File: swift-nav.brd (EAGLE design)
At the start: 53 x 53 mm, 163 parts, among them J1 SMA_EDGE, J6 ZX62-B-5PA, U1 6SLX9FTG256, U10 MAX2769, U12 PT7M8206B33TA5EX, U13 M25PX80, U2 LTC3407A_DFN, U3 STM32-M-64-LQFP, U4 7Q-16.368MBG-T, U5 SMA_PATCH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

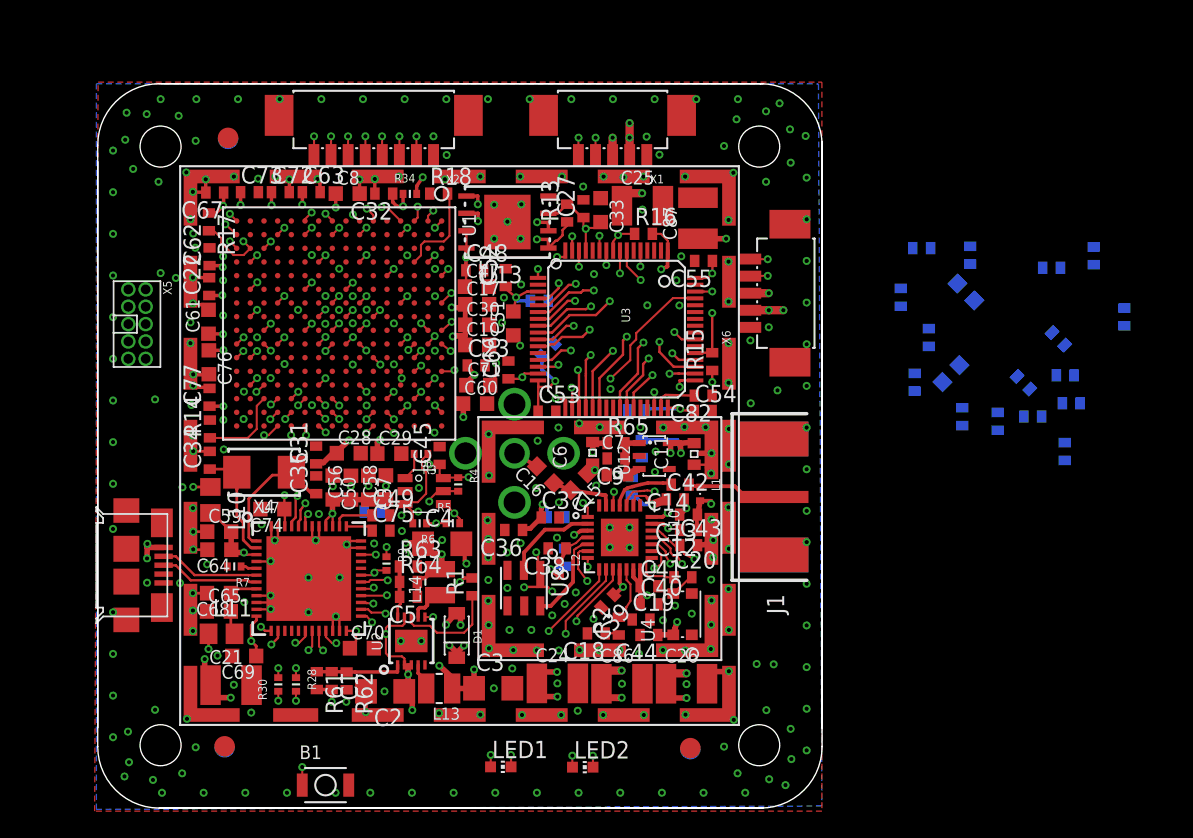
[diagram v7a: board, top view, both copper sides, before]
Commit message: Caps placed on bottom and board cleaned up a bit
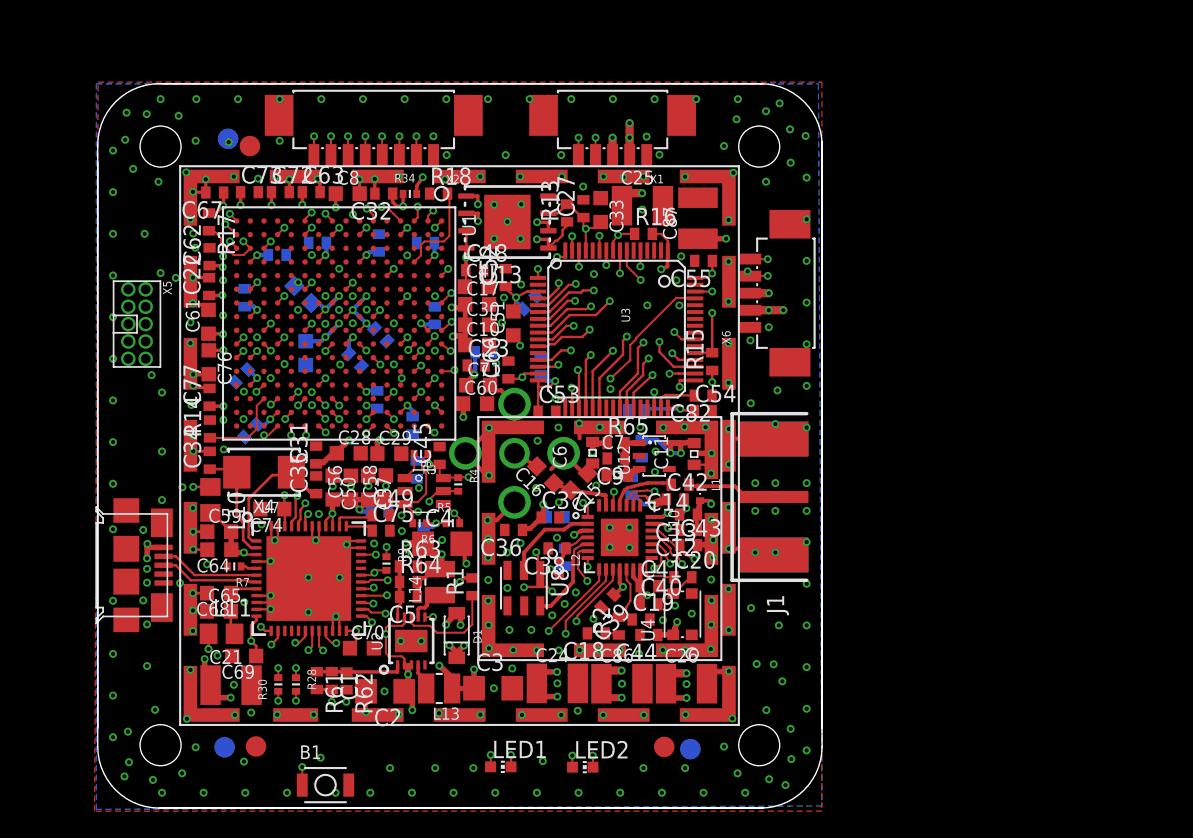
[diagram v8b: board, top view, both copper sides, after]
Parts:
- removed C95: 0.47uF, rcl:C0402
- moved C81 64.5 mm to (14.6, 31.0), turned to 315 degrees
- moved C88 61.0 mm to (14.1, 40.7), turned to 90 degrees
- moved C99 58.3 mm to (16.5, 43.9)
- moved C100 54.0 mm to (13.9, 35.0), turned to 315 degrees
- moved C98 53.5 mm to (23.9, 33.3), turned to 270 degrees
- moved C89 51.4 mm to (19.5, 44.8), turned to 0 degrees
- moved C78 49.6 mm to (24.1, 38.0)
- moved C80 48.9 mm to (22.2, 36.2)
- moved C97 48.7 mm to (27.4, 44.7)
- moved C46 48.5 mm to (18.4, 41.0)
- moved C79 47.2 mm to (18.6, 36.7), turned to 270 degrees
- moved C103 42.0 mm to (31.7, 36.8)
- moved C102 40.5 mm to (24.0, 44.7)
- moved C106 40.3 mm to (27.3, 23.3)
- moved C105 38.7 mm to (26.7, 28.2)
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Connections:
- net GND: no longer C95.2
- net VCCIO: no longer C95.1
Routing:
- net MAX_ANT_FLAG: track 112.4 -> 92.7 mm
- net GND: track 63.8 -> 81.1 mm, vias 313 -> 350
- net VCCIO: track 142.9 -> 157.0 mm, vias 75 -> 76
- net VCCINT: track 71.9 -> 82.5 mm
- net FTDI_NRST: track 113.1 -> 109.1 mm
- net FTDI_ADBUS5: track 25.6 -> 23.5 mm
- net JTAG_RST: track 93.9 -> 95.7 mm
- net FTDI_NWR: track 21.5 -> 19.8 mm
- net FTDI_ADBUS7: track 27.0 -> 25.6 mm
- net FTDI_NRXF: track 24.5 -> 23.1 mm
- net FTDI_ADBUS6: track 23.2 -> 22.0 mm
- net SPI2SCK: track 88.5 -> 87.2 mm
- net FPGA_PROGRAM_B: track 52.4 -> 51.2 mm
- net FTDI_NSIWU: track 23.3 -> 22.2 mm
- net FTDI_NTXE: track 23.2 -> 22.2 mm
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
